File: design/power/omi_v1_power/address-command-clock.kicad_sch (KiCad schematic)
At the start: 9 parts

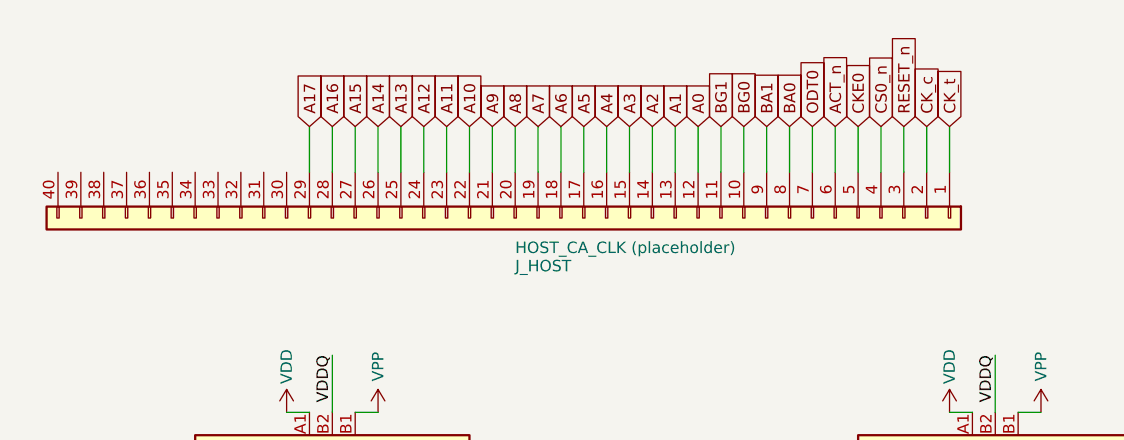
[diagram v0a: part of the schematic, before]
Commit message: feat(phase3): remove redundant J_HOST placeholder (CA/CLK/control)
J1 carries every CK/CA/control net; CK_t and CS0_n verified {J1, 8 DRAMs} after
removal. A17 (which J1 omits, per CSV "A17 NC for 8Gb") stays an 8-DRAM net,
not split. Removed symbol + 29 pin global labels (y=24.13) + 29 wire stubs;
8 DRAMs kept. ERC 100 -> 89 (acc pin_not_connected 75 -> 64; pin_not_driven
unchanged at 16, no regression).

Co-Authored-By: Claude Opus 4.8 (1M context) <noreply@anthropic.com>
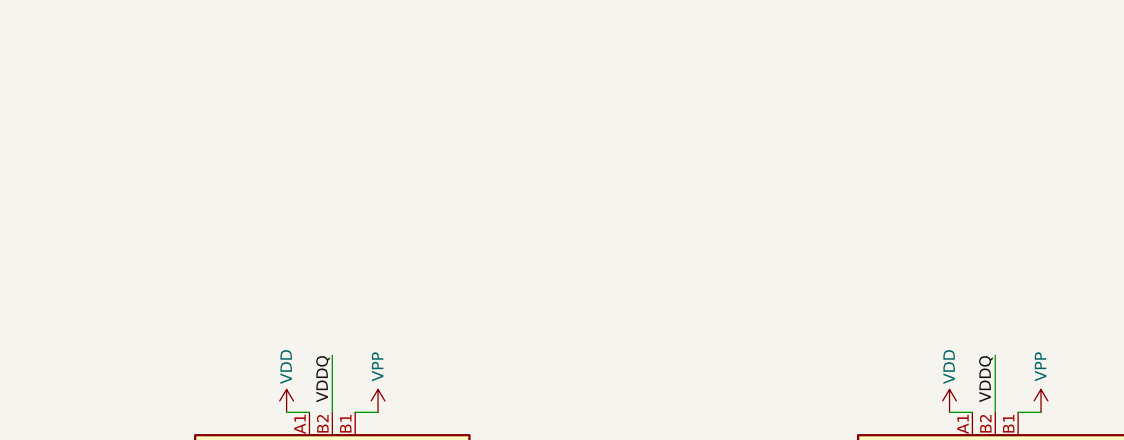
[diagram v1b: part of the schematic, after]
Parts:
- removed J_HOST: HOST_CA_CLK (placeholder), symbol Connector_Generic:Conn_01x40
